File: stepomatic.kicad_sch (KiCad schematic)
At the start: 30 parts, among them J1 I2C, J2 Conn_01x05, J4 USB_B_Micro, Q1 MMBT3904, Q2 MMBT3904, SW1 Mode, SW2 RST, U1 HDC1080DMBR, U2 AMS1117-3.3, U3 ULN2003A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

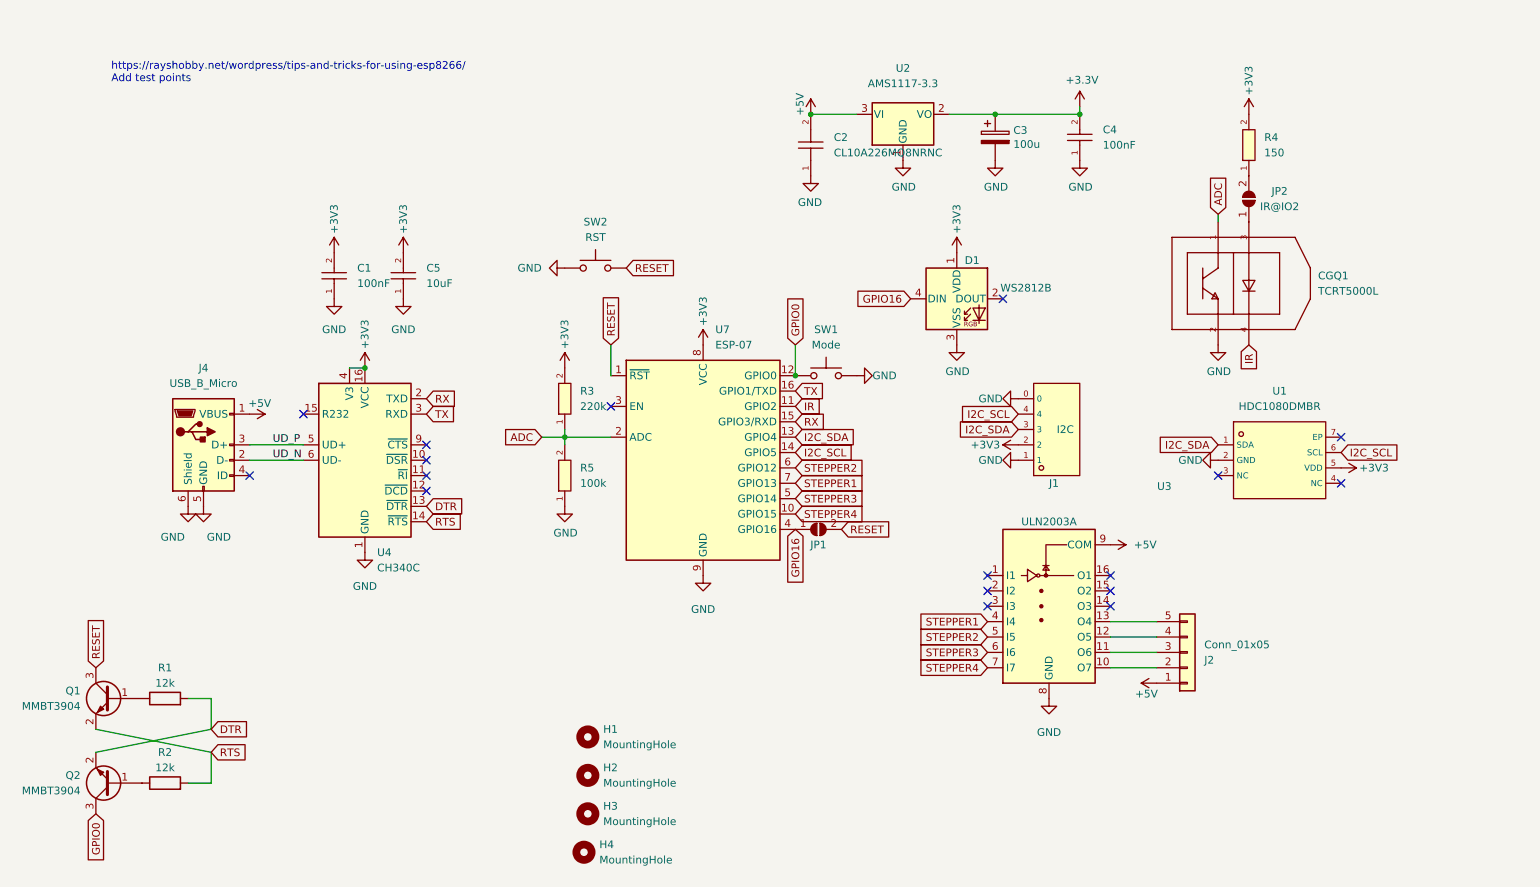
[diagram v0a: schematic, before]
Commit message: Secure 3V3 connections and change the way the ADC is read
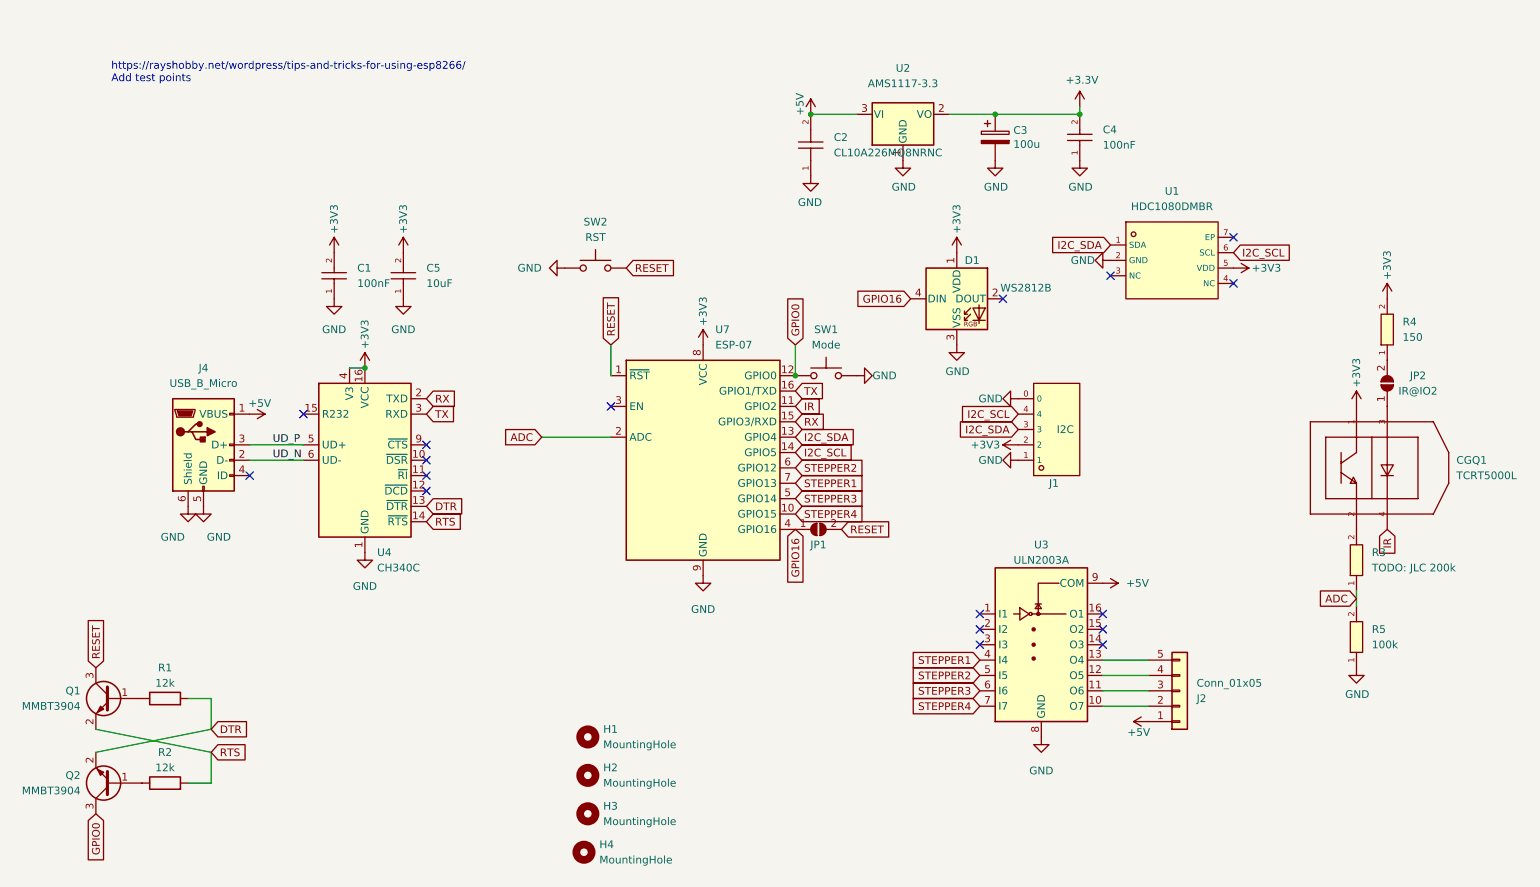
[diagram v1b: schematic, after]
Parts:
- R3: value 220k -> TODO: JLC 200k
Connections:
- net +3V3: now also CGQ1.1 (C); no longer R3.2
- net ADC: no longer CGQ1.1 (C)
- net GND: no longer CGQ1.2 (E)
- new net: CGQ1.2 (E), R3.2
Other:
- moved on the sheet: CGQ1, J2, JP2, R3, R4, R5, U1, U3

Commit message: Add 200k because of saturation voltage of the photo transistor
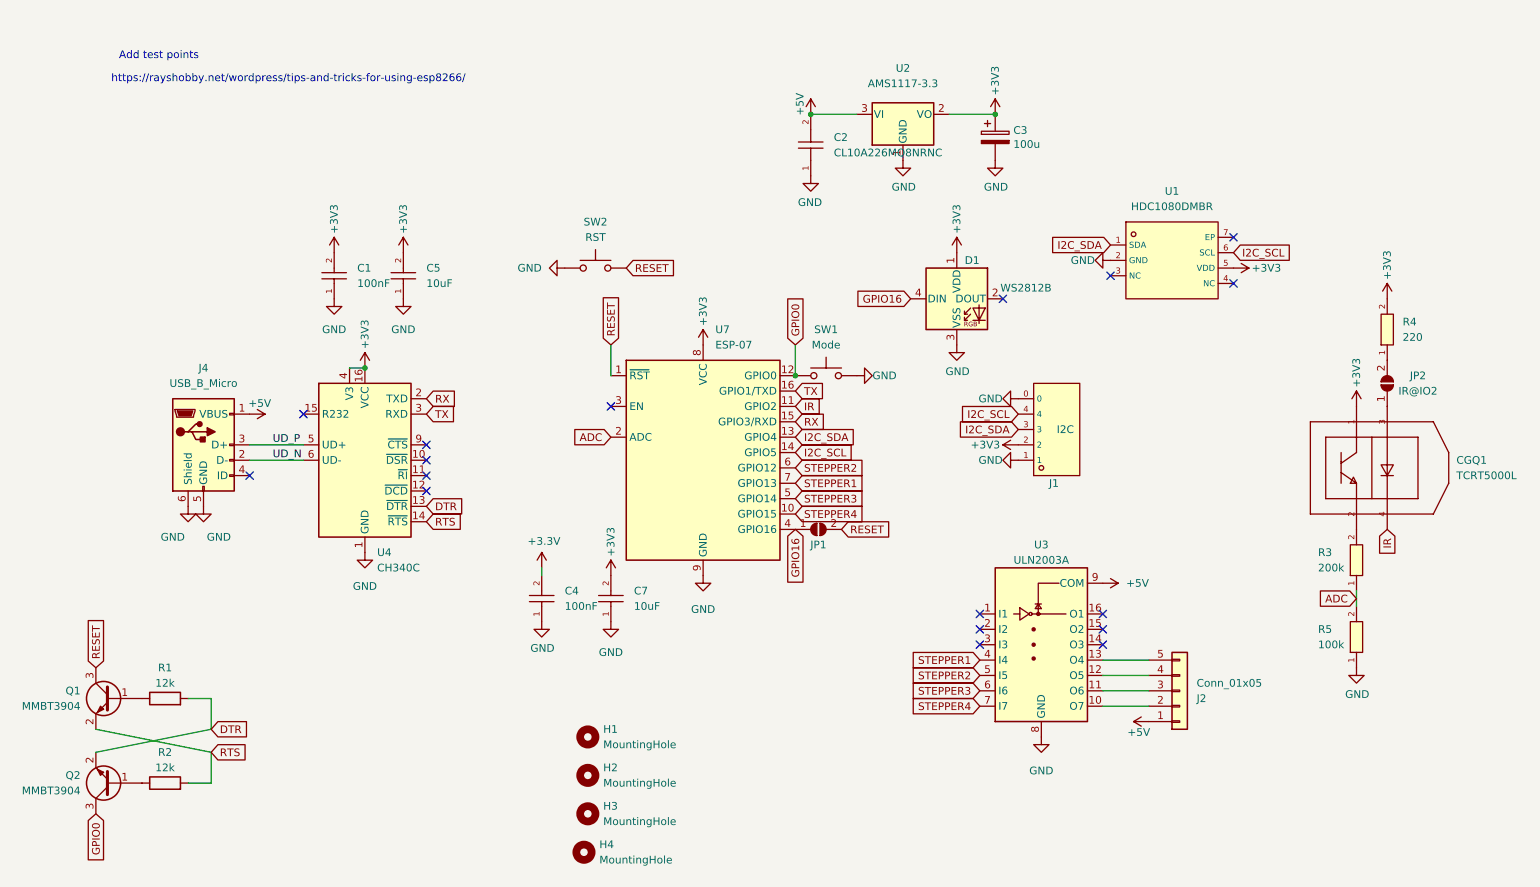
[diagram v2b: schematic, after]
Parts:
- removed R3: TODO: JLC 200k, footprint:R0603, symbol 0603WAF2203T5E:0603WAF2203T5E
- removed R4: 150, footprint:R0603, symbol 0603WAF1500T5E:0603WAF1500T5E
- added C7: 10uF, footprint:C0402, symbol CL05A106MQ5NUNC:CL05A106MQ5NUNC
- added R3: 200k, footprint:R0603, symbol 0603WAF2003T5E:0603WAF2003T5E
- added R4: 220, footprint:R0603, symbol 0603WAF2200T5E:0603WAF2200T5E
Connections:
- net +3V3: now also C7.2, R4.2
- net ADC: now also R3.1
- net GND: now also C7.1
- net at JP2.2 (B): now also R4.1
- net at CGQ1.2 (E): now also R3.2
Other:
- note added: "Add test points"
- note added: "https://rayshobby.net/wordpress/tips-and-tricks-for-using-esp8266/"
- note removed: "https://rayshobby.net/wordpress/tips-and-tricks-for-using-esp8266/ Add test points"

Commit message: Include neopixel and fix package of C3 100uF
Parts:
- D1: now in the parts list
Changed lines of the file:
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@@
   )
   (symbol (lib_id "LED:WS2812B") (at 186.69 69.85 0) (unit 1)
-    (in_bom no) (on_board yes)
+    (in_bom yes) (on_board yes)
     (property "Reference" "D1" (id 0) (at 189.23 63.5 0))
     (property "Value" "WS2812B" (id 1) (at 198.12 68.0593 0))

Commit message: Fix package of C3
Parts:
- C3: footprint footprint:CASE-B_3528 -> footprint:C1206
- J4: JLCPosOffset -0.25,0 -> -0.35,0.2
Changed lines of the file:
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@@
       (effects (font (size 1.27 1.27)) (justify left))
     )
-    (property "Footprint" "footprint:CASE-B_3528" (id 2) (at 194.0052 46.99 0)
+    (property "Footprint" "footprint:C1206" (id 2) (at 194.0052 46.99 0)
       (effects (font (size 1.27 1.27)) hide)
     )
@@
       (effects (font (size 1.27 1.27)) hide)
     )
-    (property "JLCPosOffset" "-0.25,0" (id 6) (at 62.23 93.98 0)
+    (property "JLCPosOffset" "-0.35,0.2" (id 6) (at 62.23 93.98 0)
       (effects (font (size 1.27 1.27)) hide)
     )
@@
     )
     (path "/22c9b238-cf51-4589-95ce-201c0b7ead0f"
-      (reference "C3") (unit 1) (value "100u") (footprint "footprint:CASE-B_3528")
+      (reference "C3") (unit 1) (value "100u") (footprint "footprint:C1206")
     )
     (path "/1e1a6f53-73bc-4a32-93c3-97af7a9d6dcc"

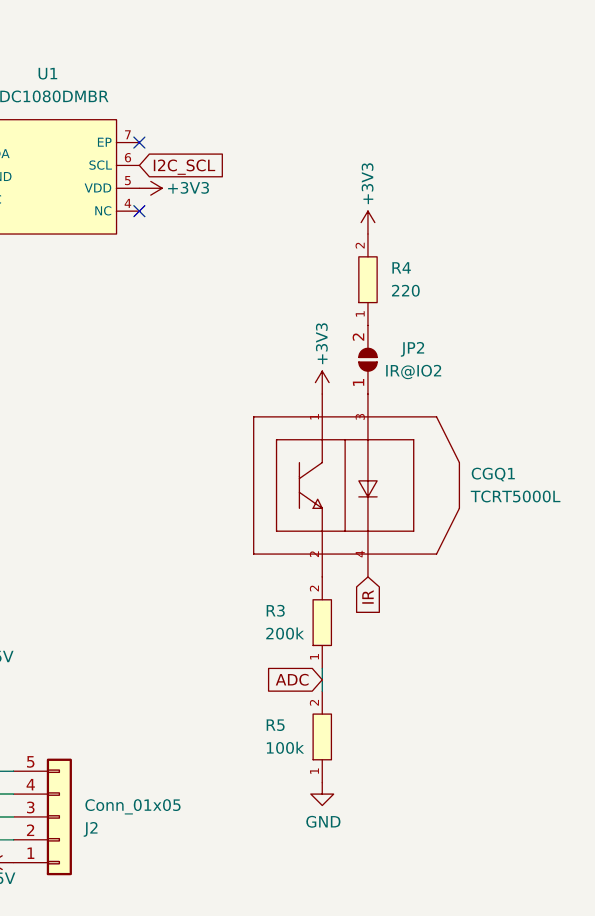
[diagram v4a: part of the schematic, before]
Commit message: Allow to switch between ON and GPIO02 for IR send
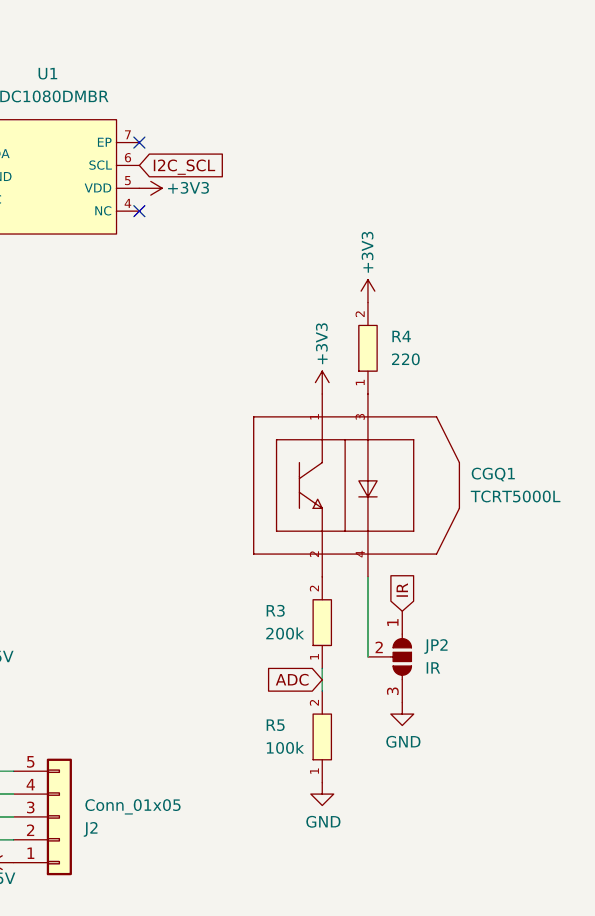
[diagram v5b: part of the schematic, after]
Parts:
- removed JP2: IR@IO2, Jumper:SolderJumper-2_P1.3mm_Open_TrianglePad1.0x1.5mm, symbol Jumper:SolderJumper_2_Open
- added JP2: IR, Jumper:SolderJumper-3_P1.3mm_Open_RoundedPad1.0x1.5mm, symbol Jumper:SolderJumper_3_Open
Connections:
- net GND: now also JP2.3 (B)
- net IR: now also JP2.1 (A); no longer CGQ1.4 (C)
- net at R4.1: now also CGQ1.3 (A)
- new net: CGQ1.4 (C), JP2.2 (C)
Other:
- moved on the sheet: R4
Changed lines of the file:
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@@
+    (stroke (width 0) (type default) (color 0 0 0 0))
+  )
+  (wire (pts (xy 257.81 107.95) (xy 257.81 116.84))
     (stroke (width 0) (type default) (color 0 0 0 0))
   )
@@
     )
   )
-  (global_label "IR" (shape input) (at 257.81 107.95 270) (fields_autoplaced)
-    (effects (font (size 1.27 1.27)) (justify right))
-    (property "Intersheet References" "${INTERSHEET_REFS}" (id 0) (at 257.7306 112.2379 90)
-      (effects (font (size 1.27 1.27)) (justify left) hide)
+  (global_label "IR" (shape input) (at 261.62 111.76 90) (fields_autoplaced)
+    (effects (font (size 1.27 1.27)) (justify left))
+    (property "Intersheet References" "${INTERSHEET_REFS}" (id 0) (at 261.6994 107.4721 90)
+      (effects (font (size 1.27 1.27)) (justify right) hide)
     )
   )
@@
     )
   )
-  (symbol (lib_id "0603WAF2200T5E:0603WAF2200T5E") (at 257.81 74.93 90) (unit 1)
-    (in_bom yes) (on_board yes) (fields_autoplaced)
-    (property "Reference" "R4" (id 0) (at 260.35 73.6599 90)
-      (effects (font (size 1.27 1.27)) (justify right))
-    )
-    (property "Value" "220" (id 1) (at 260.35 76.1999 90)
-      (effects (font (size 1.27 1.27)) (justify right))
-    )
-    (property "Footprint" "footprint:R0603" (id 2) (at 267.97 74.93 0)
+  (symbol (lib_id "0603WAF2200T5E:0603WAF2200T5E") (at 257.81 82.55 90) (unit 1)
+    (in_bom yes) (on_board yes) (fields_autoplaced)
+    (property "Reference" "R4" (id 0) (at 260.35 81.2799 90)
+      (effects (font (size 1.27 1.27)) (justify right))
+    )
+    (property "Value" "220" (id 1) (at 260.35 83.8199 90)
+      (effects (font (size 1.27 1.27)) (justify right))
+    )
+    (property "Footprint" "footprint:R0603" (id 2) (at 267.97 82.55 0)
       (effects (font (size 1.27 1.27) italic) hide)
     )
-    (property "Datasheet" "https://www.mouser.in/datasheet/2/447/PYu_RT_1_to_0_01_RoHS_L_11-1669912.pdf" (id 3) (at 257.683 77.216 0)
-      (effects (font (size 1.27 1.27)) (justify left) hide)
-    )
-    (property "LCSC" "C22962" (id 4) (at 257.81 74.93 0)
+    (property "Datasheet" "https://www.mouser.in/datasheet/2/447/PYu_RT_1_to_0_01_RoHS_L_11-1669912.pdf" (id 3) (at 257.683 84.836 0)
+      (effects (font (size 1.27 1.27)) (justify left) hide)
+    )
+    (property "LCSC" "C22962" (id 4) (at 257.81 82.55 0)
       (effects (font (size 1.27 1.27)) hide)
     )
@@
     (pin "1")
   )
-  (symbol (lib_id "Jumper:SolderJumper_2_Open") (at 257.81 83.82 90) (unit 1)
-    (in_bom no) (on_board yes)
-    (property "Reference" "JP2" (id 0) (at 262.89 82.55 90))
-    (property "Value" "IR@IO2" (id 1) (at 262.89 85.09 90))
-    (property "Footprint" "Jumper:SolderJumper-2_P1.3mm_Open_TrianglePad1.0x1.5mm" (id 2) (at 257.81 83.82 0)
-      (effects (font (size 1.27 1.27)) hide)
-    )
-    (property "Datasheet" "~" (id 3) (at 257.81 83.82 0)
-      (effects (font (size 1.27 1.27)) hide)
-    )
-    (property "LCSC" "DNP" (id 5) (at 257.81 83.82 0)
-      (effects (font (size 1.27 1.27)) hide)
-    )
-    (pin "1")
-    (pin "2")
-  )
   (symbol (lib_id "power:+5V") (at 218.44 139.7 90) (mirror x) (unit 1)
     (in_bom yes) (on_board yes)
@@
     (pin "2")
   )
-  (symbol (lib_id "power:+3V3") (at 257.81 69.85 0) (mirror y) (unit 1)
-    (in_bom yes) (on_board yes)
-    (property "Reference" "#PWR0102" (id 0) (at 257.81 73.66 0)
-      (effects (font (size 1.27 1.27)) hide)
-    )
-    (property "Value" "+3V3" (id 1) (at 257.81 61.849 90)
-      (effects (font (size 1.27 1.27)) (justify right))
-    )
-    (property "Footprint" "" (id 2) (at 257.81 69.85 0)
-      (effects (font (size 1.27 1.27)) hide)
-    )
-    (property "Datasheet" "" (id 3) (at 257.81 69.85 0)
+  (symbol (lib_id "power:+3V3") (at 257.81 77.47 0) (mirror y) (unit 1)
+    (in_bom yes) (on_board yes)
+    (property "Reference" "#PWR0102" (id 0) (at 257.81 81.28 0)
+      (effects (font (size 1.27 1.27)) hide)
+    )
+    (property "Value" "+3V3" (id 1) (at 257.81 69.469 90)
+      (effects (font (size 1.27 1.27)) (justify right))
+    )
+    (property "Footprint" "" (id 2) (at 257.81 77.47 0)
+      (effects (font (size 1.27 1.27)) hide)
+    )
+    (property "Datasheet" "" (id 3) (at 257.81 77.47 0)
       (effects (font (size 1.27 1.27)) hide)
     )
@@
     (pin "1")
   )
+  (symbol (lib_id "power:GND") (at 261.62 121.92 0) (unit 1)
+    (in_bom yes) (on_board yes)
+    (property "Reference" "#PWR0110" (id 0) (at 261.62 128.27 0)
+      (effects (font (size 1.27 1.27)) hide)
+    )
+    (property "Value" "GND" (id 1) (at 261.747 126.3142 0))
+    (property "Footprint" "" (id 2) (at 261.62 121.92 0)
+      (effects (font (size 1.27 1.27)) hide)
+    )
+    (property "Datasheet" "" (id 3) (at 261.62 121.92 0)
+      (effects (font (size 1.27 1.27)) hide)
+    )
+    (pin "1")
+  )
   (symbol (lib_id "power:GND") (at 144.78 115.57 0) (mirror y) (unit 1)
     (in_bom yes) (on_board yes) (fields_autoplaced)
@@
       (effects (font (size 1.27 1.27)) hide)
     )
+  )
+  (symbol (lib_id "Jumper:SolderJumper_3_Open") (at 261.62 116.84 270) (unit 1)
+    (in_bom yes) (on_board yes) (fields_autoplaced)
+    (property "Reference" "JP2" (id 0) (at 264.16 115.5699 90)
+      (effects (font (size 1.27 1.27)) (justify left))
+    )
+    (property "Value" "IR" (id 1) (at 264.16 118.1099 90)
+      (effects (font (size 1.27 1.27)) (justify left))
+    )
+    (property "Footprint" "Jumper:SolderJumper-3_P1.3mm_Open_RoundedPad1.0x1.5mm" (id 2) (at 261.62 116.84 0)
+      (effects (font (size 1.27 1.27)) hide)
+    )
+    (property "Datasheet" "~" (id 3) (at 261.62 116.84 0)
+      (effects (font (size 1.27 1.27)) hide)
+    )
+    (pin "1")
+    (pin "2")
+    (pin "3")
   )
   (symbol (lib_id "Mechanical:MountingHole") (at 125.73 148.59 0) (unit 1)
@@
       (reference "#PWR0109") (unit 1) (value "+5V") (footprint "")
     )
+    (path "/82dd304a-afff-49ff-84dc-de6c95d13c62"
+      (reference "#PWR0110") (unit 1) (value "GND") (footprint "")
+    )
     (path "/f79577be-2482-43ec-a3db-27da2785cb91"
       (reference "#PWR0112") (unit 1) (value "GND") (footprint "")
@@
       (reference "JP1") (unit 1) (value "Deep Sleep") (footprint "Jumper:SolderJumper-2_P1.3mm_Open_TrianglePad1.0x1.5mm")
     )
-    (path "/43e716f9-4dd6-4610-ae07-63de1d43abf8"
-      (reference "JP2") (unit 1) (value "IR@IO2") (footprint "Jumper:SolderJumper-2_P1.3mm_Open_TrianglePad1.0x1.5mm")
+    (path "/9ddabe73-a355-417b-834f-18ed5f8851a8"
+      (reference "JP2") (unit 1) (value "IR") (footprint "Jumper:SolderJumper-3_P1.3mm_Open_RoundedPad1.0x1.5mm")
     )
     (path "/3848a93b-ec2e-4c69-980c-bcbbecd16bc8"

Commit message: Tidy up
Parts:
- C2: value CL10A226MQ8NRNC -> 22u
- J2: value Conn_01x05 -> 28BYJ-48
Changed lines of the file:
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@@
       (effects (font (size 1.27 1.27)) (justify right))
     )
-    (property "Value" "CL10A226MQ8NRNC" (id 1) (at 166.37 45.7199 90)
+    (property "Value" "22u" (id 1) (at 166.37 45.7199 90)
       (effects (font (size 1.27 1.27)) (justify right))
     )
@@
       (effects (font (size 1.27 1.27)) (justify left))
     )
-    (property "Value" "Conn_01x05" (id 1) (at 226.314 133.3501 0)
+    (property "Value" "28BYJ-48" (id 1) (at 226.314 133.3501 0)
       (effects (font (size 1.27 1.27)) (justify left))
     )
@@
     )
     (path "/8eed71b8-3cc5-4192-9715-009efe80de49"
-      (reference "C2") (unit 1) (value "CL10A226MQ8NRNC") (footprint "footprint:C0603")
+      (reference "C2") (unit 1) (value "22u") (footprint "footprint:C0603")
     )
     (path "/22c9b238-cf51-4589-95ce-201c0b7ead0f"
@@
     )
     (path "/daa4d8a1-8f94-4834-94ac-ea4f5a8e3b41"
-      (reference "J2") (unit 1) (value "Conn_01x05") (footprint "footprint:CONN-TH_B5B-XH-A-LF-SN")
+      (reference "J2") (unit 1) (value "28BYJ-48") (footprint "footprint:CONN-TH_B5B-XH-A-LF-SN")
     )
     (path "/c93b24b6-f087-4eeb-a88b-a9a714a140bb"
